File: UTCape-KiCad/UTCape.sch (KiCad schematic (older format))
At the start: 6 parts, among them IC1 74LVC1G157

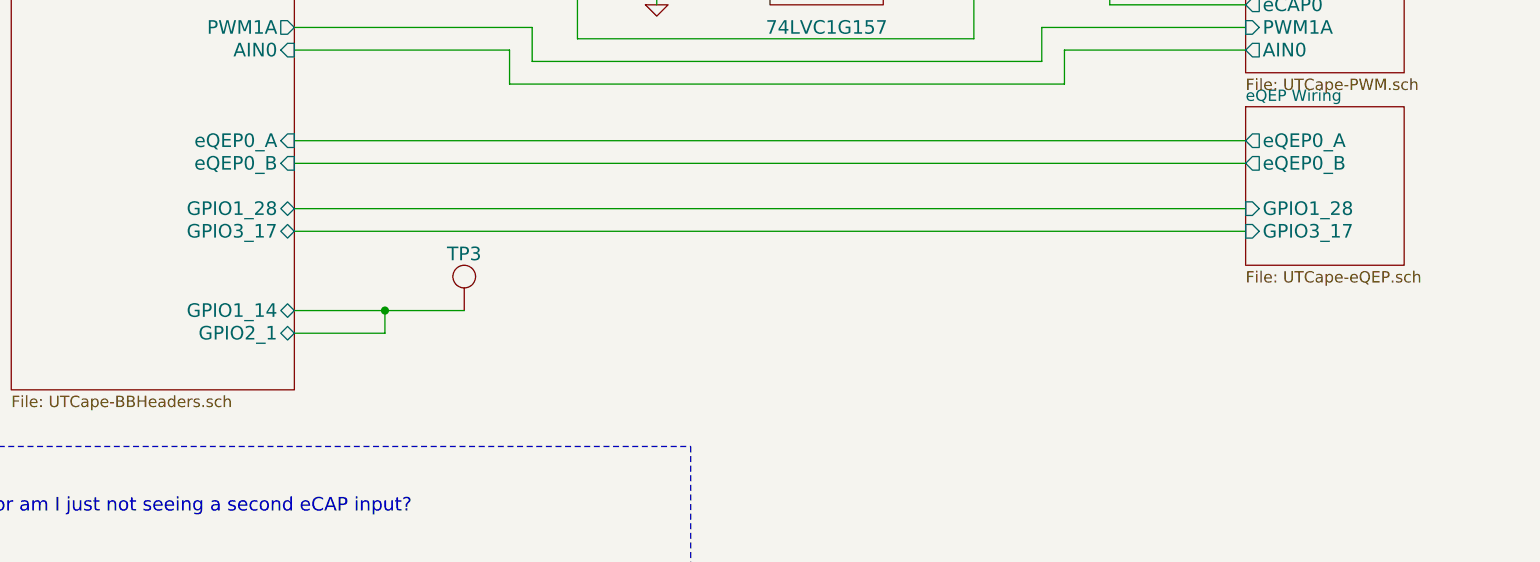
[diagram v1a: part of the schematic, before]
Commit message: added missing resistor in divider plus some protection resistors, regenerated fab files
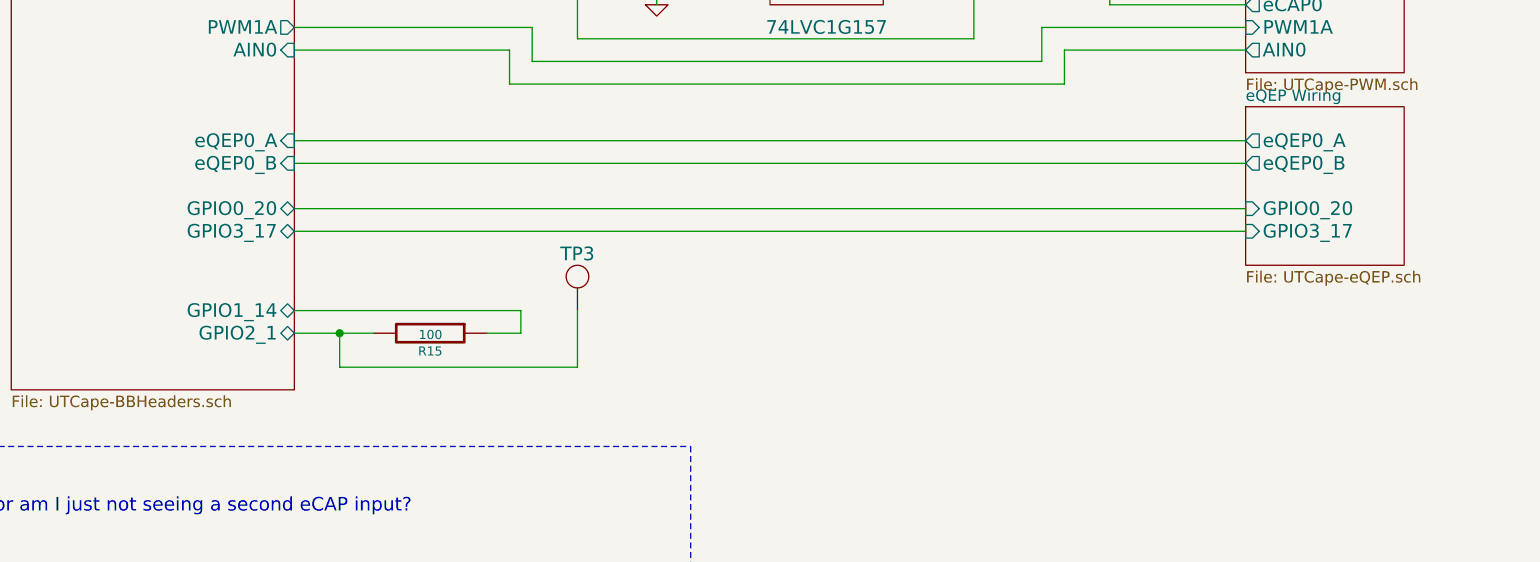
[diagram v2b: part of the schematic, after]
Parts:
- added R15: 100, ~, symbol R
- IC1: Manufacturer (none) -> NXP Semiconductors; Mfg. part num. (none) -> 74LVC1G157GW; Supplier (none) -> Digi-Key; Supplier part num. (none) -> 568-3008-1-ND
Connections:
- net BeagleBone Headers/GPIO1_14: now also R15.1; no longer TP3.1
- new net BeagleBone Headers/GPIO2_1: R15.2, TP3.1
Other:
- moved on the sheet: TP3
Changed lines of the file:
@@
 Sheet 1 9
 Title ""
-Date "24 feb 2015"
+Date "24 mar 2015"
 Rev ""
 Comp ""
@@
 F10 "AIN2" I R 3000 3500 60
 F11 "AIN0" I R 3000 4750 60
-F12 "GPIO1_28" B R 3000 5450 60
-F13 "PWM1A" O R 3000 4650 60
-F14 "I2C1_SDA" B R 3000 2700 60
-F15 "I2C2_SDA" B R 3000 3000 60
-F16 "UART2_RX" I R 3000 1300 60
-F17 "UART1_TX" O R 3000 1100 60
-F18 "UART1_RX" I R 3000 1000 60
-F19 "SPI1_CS0" O R 3000 1900 60
-F20 "SPI1_MOSI" O R 3000 2100 60
-F21 "eQEP0_A" I R 3000 5150 60
-F22 "eCAP0_IN" I R 3000 4200 60
-F23 "GPIO1_12" B R 3000 4000 60
-F24 "GPIO1_14" B R 3000 5900 60
-F25 "GPIO0_26" B R 3000 4100 60
-F26 "GPIO0_27" B R 3000 4450 60
-F27 "GPIO2_1" B R 3000 6000 60
+F12 "PWM1A" O R 3000 4650 60
+F13 "I2C1_SDA" B R 3000 2700 60
+F14 "I2C2_SDA" B R 3000 3000 60
+F15 "UART2_RX" I R 3000 1300 60
+F16 "UART1_TX" O R 3000 1100 60
+F17 "UART1_RX" I R 3000 1000 60
+F18 "SPI1_CS0" O R 3000 1900 60
+F19 "SPI1_MOSI" O R 3000 2100 60
+F20 "eQEP0_A" I R 3000 5150 60
+F21 "eCAP0_IN" I R 3000 4200 60
+F22 "GPIO1_12" B R 3000 4000 60
+F23 "GPIO1_14" B R 3000 5900 60
+F24 "GPIO0_26" B R 3000 4100 60
+F25 "GPIO0_27" B R 3000 4450 60
+F26 "GPIO2_1" B R 3000 6000 60
+F27 "GPIO0_20" B R 3000 5450 60
 $EndSheet
 $Comp
@@
 F 2 "" H 5350 4050 60  0000 C CNN
 F 3 "" H 5350 4050 60  0000 C CNN
+F 4 "NXP Semiconductors" H 5350 4350 60  0001 C CNN "Manufacturer"
+F 5 "74LVC1G157GW" H 5350 4350 60  0001 C CNN "Mfg. part num."
+F 6 "Digi-Key" H 5350 4350 60  0001 C CNN "Supplier"
+F 7 "568-3008-1-ND" H 5350 4350 60  0001 C CNN "Supplier part num."
 	1    5350 4350
 	-1   0    0    -1
@@
 	1    0    0    -1
 $EndComp
-Wire Wire Line
-	9600 1950 9600 2350
-Wire Wire Line
-	9600 2100 9250 2100
-Wire Wire Line
-	9250 2100 9250 2000
-Connection ~ 9600 2100
-Wire Wire Line
-	9600 2750 9600 3050
-Wire Wire Line
-	9000 2900 9600 2900
-Wire Wire Line
-	9250 2900 9250 2800
-Connection ~ 9600 2900
-Wire Wire Line
-	4800 4500 4600 4500
-Wire Wire Line
-	4600 4500 4600 4550
-Wire Wire Line
-	4800 4200 4600 4200
-Wire Wire Line
-	4600 4200 4600 4150
-Wire Wire Line
-	4100 4350 4800 4350
-Wire Wire Line
-	4100 4200 4100 4350
-Wire Wire Line
-	3000 4200 4100 4200
-Wire Wire Line
-	4250 4450 4250 4700
-Wire Wire Line
-	4250 4700 6000 4700
-Wire Wire Line
-	6000 4700 6000 4500
-Wire Wire Line
-	6000 4500 5900 4500
-Wire Wire Line
-	7200 4200 5900 4200
-Wire Wire Line
-	7200 4550 6600 4550
-Wire Wire Line
-	6600 4550 6600 4300
-Wire Wire Line
-	6600 4300 5900 4300
-Wire Wire Line
-	7200 4000 6000 4000
-Wire Wire Line
-	6000 4000 6000 3850
-Wire Wire Line
-	6000 3850 4200 3850
-Wire Wire Line
-	4200 3850 4200 4000
-Wire Wire Line
-	4200 4000 3000 4000
-Wire Wire Line
-	7200 4650 6300 4650
-Wire Wire Line
-	6300 4650 6300 4800
-Wire Wire Line
-	6300 4800 4050 4800
-Wire Wire Line
-	4050 4800 4050 4650
-Wire Wire Line
-	4050 4650 3000 4650
 $Sheet
 S 7200 5000 700  700
@@
 F2 "eQEP0_A" O L 7200 5150 60
 F3 "eQEP0_B" O L 7200 5250 60
-F4 "GPIO1_28" I L 7200 5450 60
-F5 "GPIO3_17" I L 7200 5550 60
+F4 "GPIO3_17" I L 7200 5550 60
+F5 "GPIO0_20" I L 7200 5450 60
 $EndSheet
-Wire Wire Line
-	3000 5150 7200 5150
-Wire Wire Line
-	3000 5250 7200 5250
-Wire Wire Line
-	3000 5450 7200 5450
-Wire Wire Line
-	3000 5550 7200 5550
-Wire Wire Line
-	3000 3100 7200 3100
-Wire Wire Line
-	3000 3000 7200 3000
-Wire Wire Line
-	3000 2800 7200 2800
-Wire Wire Line
-	3000 2700 7200 2700
-Wire Wire Line
-	3000 2200 7200 2200
-Wire Wire Line
-	3000 2100 7200 2100
-Wire Wire Line
-	3000 2000 7200 2000
-Wire Wire Line
-	3000 1900 7200 1900
-Wire Wire Line
-	3000 1400 7200 1400
-Wire Wire Line
-	3000 1300 7200 1300
-Wire Wire Line
-	3000 1100 7200 1100
-Wire Wire Line
-	3000 1000 7200 1000
 $Comp
 L TEST_POINT TP3
 U 1 1 54F05C31
-P 3750 5900
-F 0 "TP3" H 3750 6150 60  0000 C CNN
-F 1 "TEST_POINT" H 3450 5950 60  0001 C CNN
-F 2 "" H 3750 5900 60  0000 C CNN
-F 3 "" H 3750 5900 60  0000 C CNN
-	1    3750 5900
+P 4250 5900
+F 0 "TP3" H 4250 6150 60  0000 C CNN
+F 1 "TEST_POINT" H 3950 5950 60  0001 C CNN
+F 2 "" H 4250 5900 60  0000 C CNN
+F 3 "" H 4250 5900 60  0000 C CNN
+	1    4250 5900
 	1    0    0    -1
 $EndComp
@@
 53 DD DB 70 1F 36 16 E8 FD 00 E2 DF AD 51 CE 83 A6 28 F1 7F 81 8B E0 02 2E 82 F7 7A 32 7C 03 A2
 99 A9 ED 10 75 E1 56 1A 44 BB 99 51 9D 33 AA 2F 6B B6 E7 B9 1B FC 3F 2A D6 C2 F1 E6 45 93 97 00
-00 00 00 49 45 4E 44 AE 42 60 82 86 $EndBitmap
+00 00 00 49 45 4E 44 AE 42 60 82 A0 $EndBitmap
 EndData
 $EndBitmap
@@
 03 43 83 61 8C 09 03 03 03 03 43 83 61 8C 09 03 03 03 03 43 83 61 8C 09 03 03 03 03 43 83 61 03
 60 D2 64 32 30 30 30 30 34 84 CF 1C 00 A9 00 9C 01 A8 8B 59 19 06 06 06 06 06 E9 E3 33 80 C5 FF
-07 47 25 A5 D2 E9 03 52 D8 00 00 00 00 49 45 4E 44 AE 42 60 82 4A $EndBitmap
+07 47 25 A5 D2 E9 03 52 D8 00 00 00 00 49 45 4E 44 AE 42 60 82 CF $EndBitmap
 EndData
 $EndBitmap
@@
 Text Notes 600  6650 0    60   ~ 12
 Notes:
-Wire Notes Line
-	550  6500 4750 6500
-Wire Notes Line
-	4750 6500 4750 7700
 Text Notes 700  6800 0    60   ~ 0
 1. Is IC1 really needed, or am I just not seeing a second eCAP input?
@@
 	1    0    0    -1
 $EndComp
+$Comp
+L R R15
+U 1 1 54F67430
+P 3600 6000
+F 0 "R15" V 3680 6000 40  0000 C CNN
+F 1 "100" V 3607 6001 40  0000 C CNN
+F 2 "~" V 3530 6000 30  0000 C CNN
+F 3 "~" H 3600 6000 30  0000 C CNN
+	1    3600 6000
+	0    1    1    0
+$EndComp
+Wire Wire Line
+	9600 1950 9600 2350
+Wire Wire Line
+	9600 2100 9250 2100
+Wire Wire Line
+	9250 2100 9250 2000
+Connection ~ 9600 2100
+Wire Wire Line
+	9600 2750 9600 3050
+Wire Wire Line
+	9000 2900 9600 2900
+Wire Wire Line
+	9250 2900 9250 2800
+Connection ~ 9600 2900
+Wire Wire Line
+	4800 4500 4600 4500
+Wire Wire Line
+	4600 4500 4600 4550
+Wire Wire Line
+	4800 4200 4600 4200
+Wire Wire Line
+	4600 4200 4600 4150
+Wire Wire Line
+	4100 4350 4800 4350
+Wire Wire Line
+	4100 4200 4100 4350
+Wire Wire Line
+	3000 4200 4100 4200
+Wire Wire Line
+	4250 4450 4250 4700
+Wire Wire Line
+	4250 4700 6000 4700
+Wire Wire Line
+	6000 4700 6000 4500
+Wire Wire Line
+	6000 4500 5900 4500
+Wire Wire Line
+	7200 4200 5900 4200
+Wire Wire Line
+	7200 4550 6600 4550
+Wire Wire Line
+	6600 4550 6600 4300
+Wire Wire Line
+	6600 4300 5900 4300
+Wire Wire Line
+	7200 4000 6000 4000
+Wire Wire Line
+	6000 4000 6000 3850
+Wire Wire Line
+	6000 3850 4200 3850
+Wire Wire Line
+	4200 3850 4200 4000
+Wire Wire Line
+	4200 4000 3000 4000
+Wire Wire Line
+	7200 4650 6300 4650
+Wire Wire Line
+	6300 4650 6300 4800
+Wire Wire Line
+	6300 4800 4050 4800
+Wire Wire Line
+	4050 4800 4050 4650
+Wire Wire Line
+	4050 4650 3000 4650
+Wire Wire Line
+	3000 5150 7200 5150
+Wire Wire Line
+	3000 5250 7200 5250
+Wire Wire Line
+	3000 5550 7200 5550
+Wire Wire Line
+	3000 3100 7200 3100
+Wire Wire Line
+	3000 3000 7200 3000
+Wire Wire Line
+	3000 2800 7200 2800
+Wire Wire Line
+	3000 2700 7200 2700
+Wire Wire Line
+	3000 2200 7200 2200
+Wire Wire Line
+	3000 2100 7200 2100
+Wire Wire Line
+	3000 2000 7200 2000
+Wire Wire Line
+	3000 1900 7200 1900
+Wire Wire Line
+	3000 1400 7200 1400
+Wire Wire Line
+	3000 1300 7200 1300
+Wire Wire Line
+	3000 1100 7200 1100
+Wire Wire Line
+	3000 1000 7200 1000
+Wire Notes Line
+	550  6500 4750 6500
+Wire Notes Line
+	4750 6500 4750 7700
 Wire Wire Line
 	9000 2900 9000 2800
@@
 	4300 4100 3000 4100
 Wire Wire Line
-	3000 5900 3750 5900
-Wire Wire Line
-	3000 6000 3400 6000
-Wire Wire Line
-	3400 6000 3400 5900
-Connection ~ 3400 5900
-Wire Wire Line
 	3000 3500 7200 3500
 Wire Wire Line
@@
 Wire Wire Line
 	6400 4750 7200 4750
+Wire Wire Line
+	3000 6000 3350 6000
+Wire Wire Line
+	3850 6000 4000 6000
+Wire Wire Line
+	4000 6000 4000 5900
+Wire Wire Line
+	4000 5900 3000 5900
+Wire Wire Line
+	4250 5900 4250 6150
+Wire Wire Line
+	4250 6150 3200 6150
+Wire Wire Line
+	3200 6150 3200 6000
+Connection ~ 3200 6000
+Wire Wire Line
+	7200 5450 3000 5450
 $EndSCHEMATC
